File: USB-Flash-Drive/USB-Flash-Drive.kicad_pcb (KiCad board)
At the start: 2 copper layers, 19.4 x 49.1 mm, 37 parts, among them J1 USB_A, J2 Conn_01x03_Pin, U1 RP2040, U2 W25Q128JVS, U3 AMS1117, U4 W25N01GVZEIG, Y2 ABM8-272-T3

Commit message: Thumb Drive First Manufacturing Attempt
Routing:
- net Net-(U1-USB_DP): track 28.0 -> 30.1 mm
- net GND: vias 15 -> 20
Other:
- board text added: "128MB Thumb Drive v1.0.0"
- board text added: "Designed by: Cooper Werner"

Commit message: USB-Thumb-Drive V2
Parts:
- added G***: LOGO, LOGO, B.Cu at (112.3, 137.9)
- C1, C13, C14, C3: footprint Capacitor_SMD:C_0201_0603Metric -> Capacitor_SMD:C_0402_1005Metric
- C10, C15, C16, C2, C4, C5, C6, C7, C8, C9: footprint Capacitor_SMD:C_01005_0402Metric -> Capacitor_SMD:C_0402_1005Metric
- U2: footprint Package_SO:SOIC-8_5.23x5.23mm_P1.27mm -> Package_SO:SOIC-8_5.3x5.3mm_P1.27mm
- moved C8 82.3 mm to (107.4, 143.8), turned to 90 degrees
- moved C16 81.7 mm to (103.2, 134.5), turned to 0 degrees
- moved R7 80.8 mm to (108.3, 114.6), turned to 0 degrees
- moved R4 79.0 mm to (102.8, 126.5), turned to 0 degrees
- moved R8 78.9 mm to (99.9, 140.1), turned to 90 degrees
- moved C5 77.9 mm to (111.6, 132.3), turned to -90 degrees
- moved D1 77.6 mm to (100.4, 135.4)
- moved D2 77.6 mm to (100.4, 136.5)
- moved D3 77.6 mm to (100.4, 137.5)
- moved D4 77.5 mm to (100.4, 138.5)
- moved C9 77.4 mm to (102.9, 139.0)
- moved C10 77.3 mm to (108.4, 143.8)
- moved U1 76.8 mm to (108.0, 138.0)
- moved C4 76.7 mm to (113.1, 135.5)
- moved U3 76.6 mm to (108.8, 120.9)
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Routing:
- net IOVDD: track 92.2 -> 120.2 mm, vias 8 -> 2
- net GND: track 20.6 -> 1.70 mm, vias 20 -> 172
- net Net-(J2-Pin_3): track 22.5 -> 7.07 mm, vias 1 -> 0
- net Net-(J2-Pin_2): track 18.7 -> 9.11 mm, vias 1 -> 0
- net USBD+: track 11.0 -> 2.12 mm, vias 2 -> 0
- net USBD-: track 9.76 -> 2.12 mm
- net /SPI_COPI: track 11.5 -> 18.6 mm, vias 0 -> 2
- net Net-(U1-USB_DP): track 30.1 -> 24.1 mm
- net Net-(U1-USB_DM): track 19.6 -> 25.0 mm
- net /SPI_CS: track 11.1 -> 6.01 mm, vias 0 -> 2
- net /SPI_CIPO: track 11.1 -> 6.45 mm
- net /XOUT: track 10.3 -> 6.32 mm
- net DVDD: track 33.7 -> 29.9 mm
- net /RESET: track 6.36 -> 9.98 mm, vias 1 -> 0
- net /SPI_CLK: track 13.0 -> 16.1 mm
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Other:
- board size 19.4 x 49.1 mm -> 19.8 x 47.3 mm
- board text added: "128MB USB Flash Drive"
- board text removed: "128MB Thumb Drive v1.0.0"
- board text removed: "Designed by: Cooper Werner"

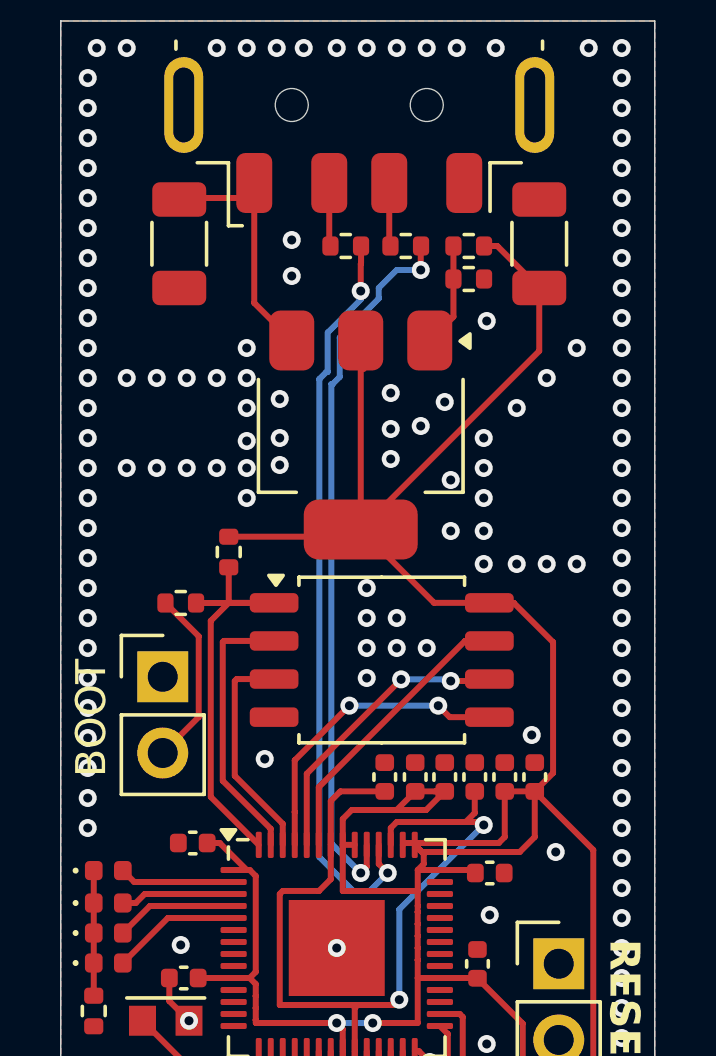
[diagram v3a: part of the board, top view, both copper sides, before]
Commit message: USB-Flash-Drive Production Ready
The flash drive is production ready, but it costs too much to produce right now

Will wait until I have the proper tools and supplies at school
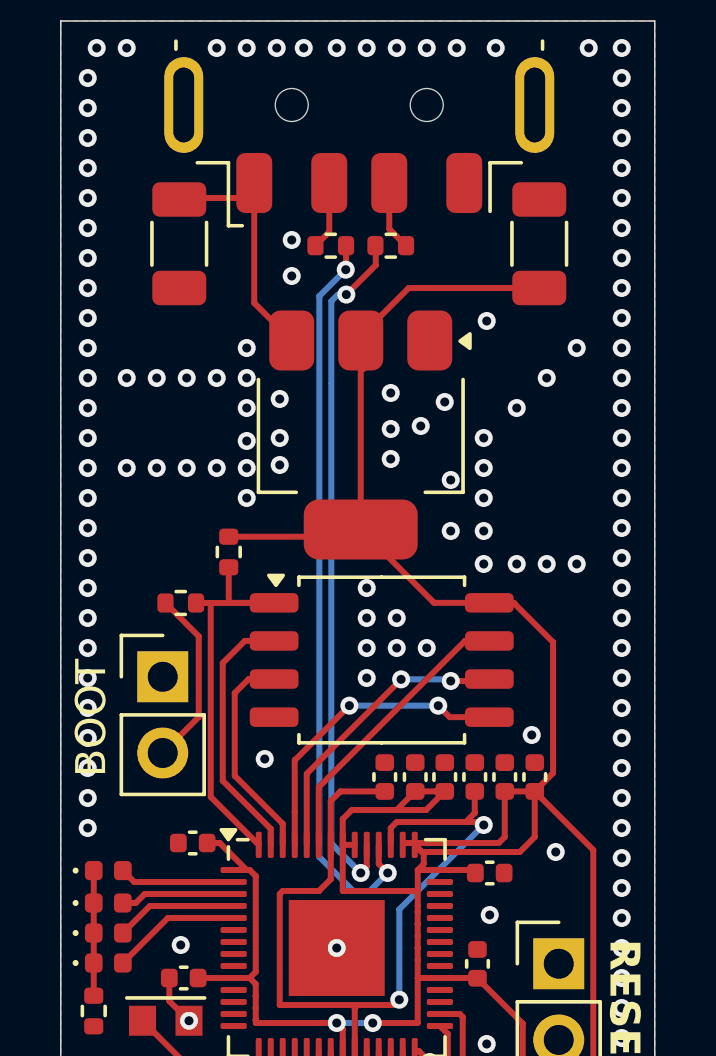
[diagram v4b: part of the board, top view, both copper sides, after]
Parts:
- removed R1: 1.6K, Resistor_SMD:R_0402_1005Metric
- removed R2: 1K, Resistor_SMD:R_0402_1005Metric
- U3: value AMS1117 -> AMS1117-3.3
- moved G*** 8.23 mm to (113.4, 129.8)
- moved R6 0.50 mm to (109.8, 114.6), turned to 180 degrees
- moved R7 0.50 mm to (107.8, 114.6)
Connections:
- U3 pad 1: Net-(U3-ADJ) -> GND
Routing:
- net IOVDD: track 120.2 -> 114.1 mm
- net Net-(U3-ADJ): track 3.48 -> 0.00 mm
- net Net-(U1-USB_DP): track 24.1 -> 23.1 mm
